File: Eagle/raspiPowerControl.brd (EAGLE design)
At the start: 33.1 x 30.6 mm, 17 parts, among them IC1 MCP1702/3 3.3, Q1 FDN360P, T1 BC847

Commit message: Update layout
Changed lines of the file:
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@@
 <wire x1="-0.127" y1="30.597" x2="0" y2="0" width="0" layer="20"/>
 <text x="26.67" y="6.858" size="1.4224" layer="26" rot="MR90">Q1</text>
-<text x="10.414" y="8.382" size="1.27" layer="25">RPi PwrSw V1
+<text x="12.446" y="9.398" size="1.27" layer="25">RPi PwrSw V1
 CZ 2023</text>
 <text x="3.556" y="12.7" size="1.016" layer="22" rot="MR0">GND</text>
@@
 <vertex x="19.939" y="22.987"/>
 </polygon>
-<via x="29.591" y="11.811" extent="1-16" drill="0.35"/>
-<via x="31.369" y="12.065" extent="1-16" drill="0.35"/>
-<via x="30.48" y="12.7" extent="1-16" drill="0.35"/>
-<via x="31.75" y="10.922" extent="1-16" drill="0.35"/>
-<via x="31.877" y="9.906" extent="1-16" drill="0.35"/>
-<via x="30.734" y="9.906" extent="1-16" drill="0.35"/>
+<via x="30.734" y="12.065" extent="1-16" drill="0.35"/>
+<via x="31.877" y="12.065" extent="1-16" drill="0.35"/>
+<via x="31.877" y="11.049" extent="1-16" drill="0.35"/>
+<via x="31.877" y="10.033" extent="1-16" drill="0.35"/>
+<via x="30.734" y="10.033" extent="1-16" drill="0.35"/>
 <via x="30.734" y="11.049" extent="1-16" drill="0.35"/>
 <polygon width="0.3048" layer="16" rank="2">
@@
 <vertex x="29.21" y="11.938"/>
 </polygon>
+<wire x1="28.448" y1="18.542" x2="30.48" y2="17.841" width="0" layer="19" extent="16-16"/>
+<wire x1="28.618" y1="19.624" x2="28.448" y2="18.542" width="0" layer="19" extent="16-16"/>
+<wire x1="27.178" y1="18.542" x2="28.448" y2="18.542" width="0" layer="19" extent="1-1"/>
+<wire x1="27.051" y1="21.59" x2="28.618" y2="19.624" width="0" layer="19" extent="16-16"/>
+<wire x1="23.622" y1="22.098" x2="27.051" y2="21.59" width="0" layer="19" extent="16-16"/>
+<wire x1="23.622" y1="19.558" x2="23.622" y2="22.098" width="0" layer="19" extent="16-16"/>
+<wire x1="22.479" y1="18.034" x2="23.622" y2="19.558" width="0" layer="19" extent="16-16"/>
+<wire x1="20.955" y1="18.034" x2="22.479" y2="18.034" width="0" layer="19" extent="1-1"/>
+<wire x1="20.447" y1="19.431" x2="20.955" y2="18.034" width="0" layer="19" extent="1-1"/>
+<wire x1="19.939" y1="20.701" x2="20.447" y2="19.431" width="0" layer="19" extent="1-1"/>
+<wire x1="19.939" y1="21.971" x2="19.939" y2="20.701" width="0" layer="19" extent="1-1"/>
+<wire x1="16.891" y1="21.717" x2="19.939" y2="21.971" width="0" layer="19" extent="16-16"/>
+<wire x1="31.877" y1="12.065" x2="30.48" y2="17.841" width="0" layer="19" extent="16-16"/>
+<wire x1="30.734" y1="11.049" x2="31.877" y2="12.065" width="0" layer="19" extent="1-1"/>
+<wire x1="31.877" y1="11.049" x2="30.734" y2="11.049" width="0" layer="19" extent="1-1"/>
+<wire x1="31.877" y1="10.033" x2="31.877" y2="11.049" width="0" layer="19" extent="1-1"/>
+<wire x1="30.734" y1="10.033" x2="30.734" y2="11.049" width="0" layer="19" extent="1-1"/>
+<wire x1="29.652" y1="10.244" x2="30.734" y2="10.033" width="0" layer="19" extent="16-16"/>
+<wire x1="30.734" y1="12.065" x2="30.734" y2="11.049" width="0" layer="19" extent="1-1"/>
 </signal>
 <signal name="N$1">

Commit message: Update layout
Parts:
- moved R2 3.14 mm to (31.2, 13.8), turned to 270 degrees
- moved R1 1.02 mm to (27.8, 17.0)
- moved D1 0.57 mm to (30.0, 21.1)
- moved J2 0.25 mm to (2.67, 27.3)
- moved T1 0.13 mm to (27.7, 13.7)
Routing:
- net SWPWR: track 24.5 -> 25.3 mm
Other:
- board text added: "RPi PwrSw V2 CZ 2023"
- board text removed: "RPi PwrSw V1 CZ 2023"

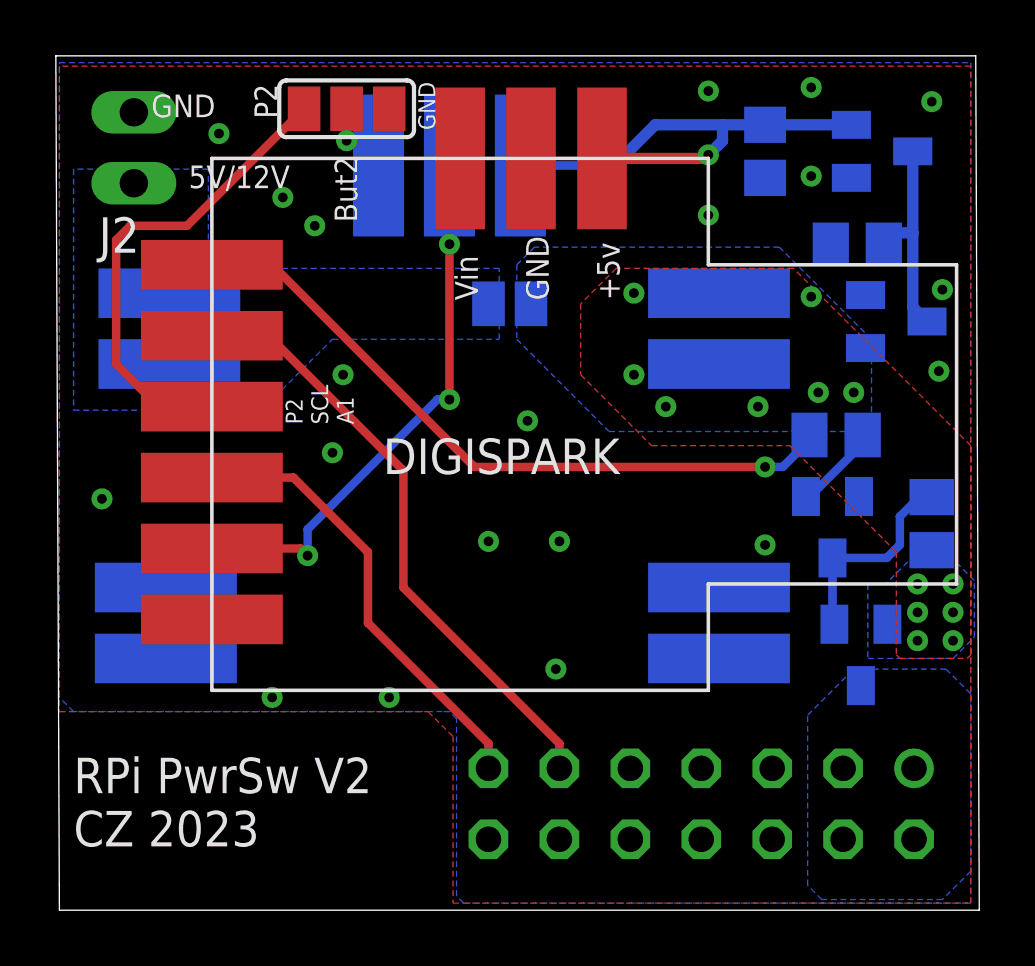
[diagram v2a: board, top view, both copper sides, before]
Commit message: Update board size and touch sensor thresh
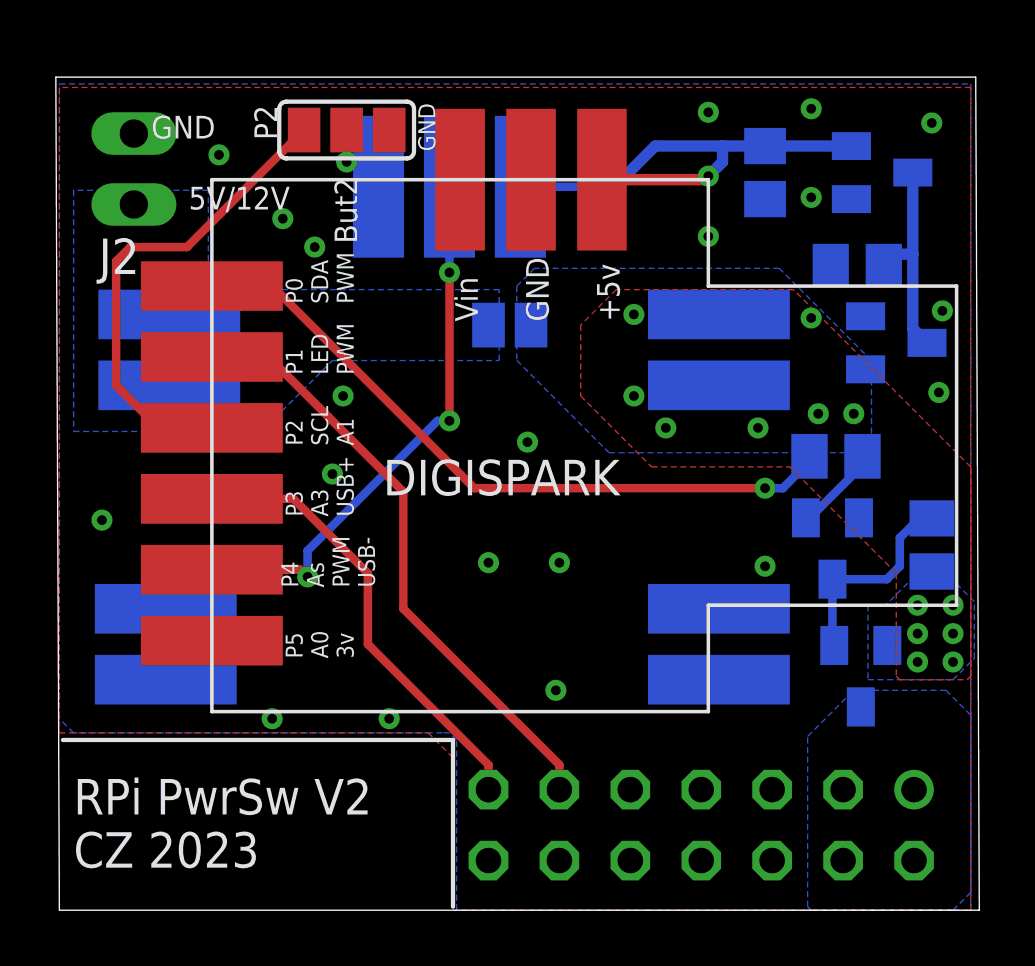
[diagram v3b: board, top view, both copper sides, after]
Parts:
- moved 3.3V 0.76 mm to (16.5, 25.9)
- moved C1 0.76 mm to (25.3, 26.4)
- moved C3 0.76 mm to (28.6, 23.1)
- moved D1 0.76 mm to (30.0, 20.3)
- moved IC1 0.76 mm to (29.5, 26.4)
- moved J2 0.76 mm to (2.67, 26.5)
- moved MP1584 0.76 mm to (13.5, 11.6)
- moved P2 0.76 mm to (10.3, 27.9)
- moved P2/GND 0.76 mm to (11.4, 25.9)
- moved P4 0.76 mm to (14.0, 25.9)
- moved PWR=5V 0.76 mm to (16.1, 21.0)
- moved Q1 0.76 mm to (28.7, 8.38)
- moved R1 0.76 mm to (27.8, 16.3)
- moved R2 0.76 mm to (31.2, 13.1)
- moved SV1 0.76 mm to (23.0, 3.05)
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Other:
- board size 33.1 x 30.6 mm -> 33.1 x 29.8 mm
